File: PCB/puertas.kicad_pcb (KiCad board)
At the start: 2 copper layers, 135.8 x 85.8 mm, 70 parts, among them IC1 MAX3051ESA+, IC2 IR2175STRPBF, J1 DE9_Pins_MountingHoles, J12 motor_dc, J2 ICSP, J3 DE9_Plug_MountingHoles, J4 Conn_Coaxial, J5 BAT_CONN, J6 Conn_01x03, J7 DOOR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

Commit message: layout pre
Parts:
- moved D5 6.83 mm to (148.8, 109.5)
- moved C10 4.21 mm to (152.7, 105.2)
- moved C13 3.89 mm to (157.5, 102.9)
- moved C9 3.75 mm to (176.8, 83.1)
- moved R9 1.52 mm to (127.3, 126.0), turned to -90 degrees
- moved R2 1.04 mm to (166.1, 117.3)
- moved R17 0.86 mm to (171.2, 74.9)
- moved R12 0.65 mm to (149.1, 74.7), turned to 180 degrees
- moved R10 0.39 mm to (117.5, 62.7)
- moved R16 0.06 mm to (159.3, 74.9)
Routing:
- net /motores/DC2: track 0.00 -> 58.2 mm
- net UP: track 0.00 -> 52.7 mm
- net CLOSE: track 0.00 -> 52.1 mm
- net DOWN: track 0.00 -> 50.7 mm
- net OPEN: track 0.00 -> 47.5 mm
- net Net-(Q3-G): track 0.00 -> 41.7 mm
- net Net-(D5-K): track 0.00 -> 41.4 mm
- net GND: track 0.00 -> 37.2 mm, vias 0 -> 30
- net Net-(IC2-VIN+): track 0.00 -> 34.8 mm, vias 0 -> 1
- net Net-(Q2-G): track 0.00 -> 32.7 mm
- net Net-(Q1-G): track 0.00 -> 31.5 mm
- net Net-(D4-K): track 0.00 -> 29.2 mm, vias 0 -> 2
- net Net-(D2-K): track 6.26 -> 34.4 mm
- net /motores/LIN2: track 0.00 -> 26.3 mm
- net Net-(Q4-G): track 0.00 -> 25.4 mm
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
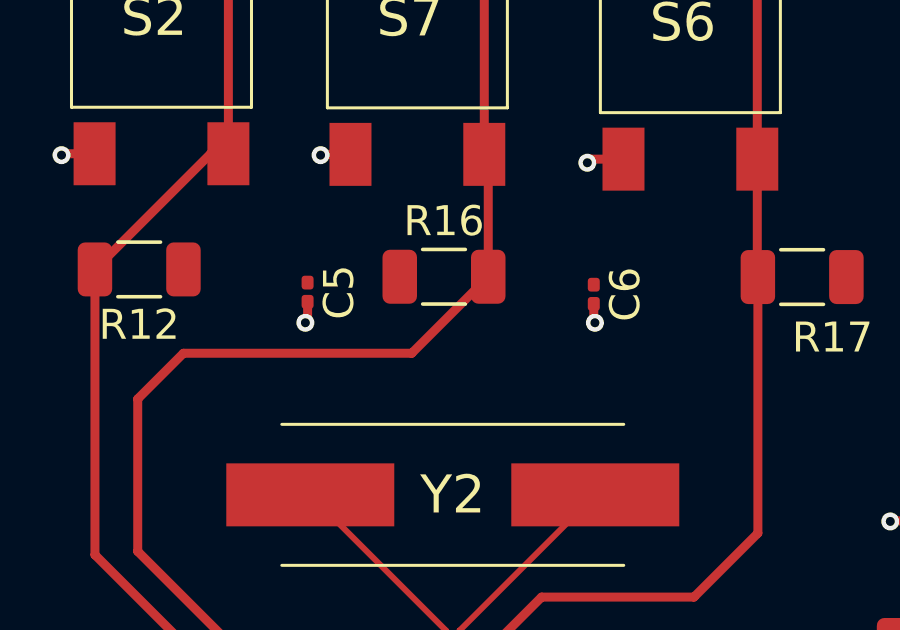
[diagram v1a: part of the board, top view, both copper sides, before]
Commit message: Fixed labels and ERC errors
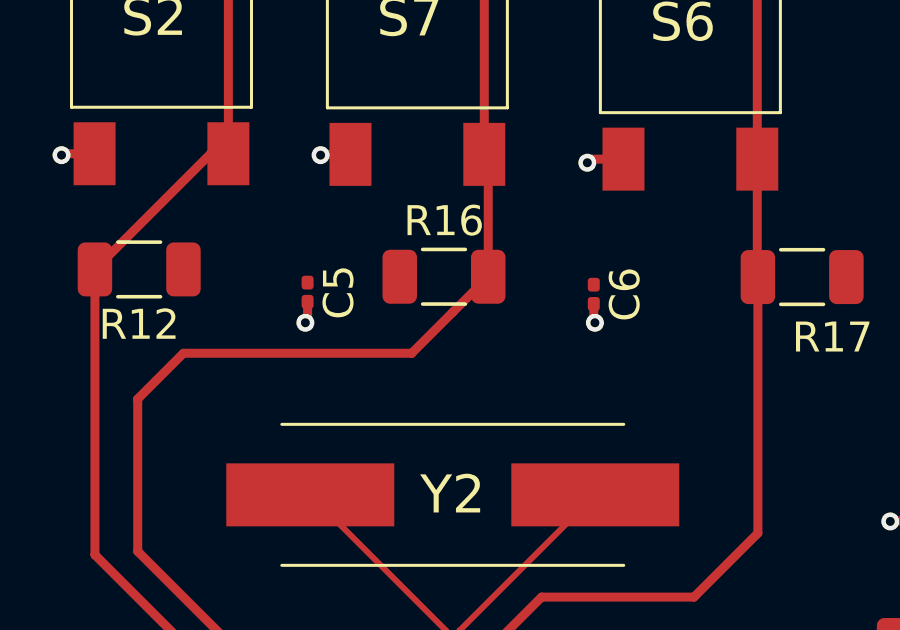
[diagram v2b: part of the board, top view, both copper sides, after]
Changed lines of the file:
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@@
 			(psa4output no)
 			(plot_black_and_white yes)
+			(plotinvisibletext no)
 			(sketchpadsonfab no)
 			(plotpadnumbers no)
@@
 	)
 	(segment
-		(start 162.56 85.598)
-		(end 159.77 88.388)
+		(start 169.77 74.93)
+		(end 169.77 83.468)
 		(width 0.3)
 		(layer "F.Cu")
@@
 	)
 	(segment
-		(start 169.77 74.93)
-		(end 169.77 83.468)
-		(width 0.3)
-		(layer "F.Cu")
-		(net 52)
-	)
-	(segment
-		(start 169.77 83.468)
-		(end 167.64 85.598)
+		(start 162.56 85.598)
+		(end 159.77 88.388)
 		(width 0.3)
 		(layer "F.Cu")
@@
 	)
 	(segment
+		(start 169.77 83.468)
+		(end 167.64 85.598)
+		(width 0.3)
+		(layer "F.Cu")
+		(net 52)
+	)
+	(segment
 		(start 169.75 74.91)
 		(end 169.77 74.93)
@@
 	(segment
 		(start 160.782 74.92)
-		(end 158.232 77.47)
+		(end 159.601 76.101)
 		(width 0.3)
 		(layer "F.Cu")
@@
 		(width 0.3)
 		(layer "F.Cu")
+		(net 54)
+	)
+	(segment
+		(start 159.601 76.101)
+		(end 158.232 77.47)
+		(width 0.3)
+		(layer "F.Cu")

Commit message: ADDED footprint RFID lector
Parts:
- added J10: Conn_01x03, Connector_PinHeader_2.54mm:PinHeader_1x03_P2.54mm_Vertical, F.Cu at (218.4, 49.5)
- added J11: Conn_01x03, Connector_PinHeader_2.54mm:PinHeader_1x03_P2.54mm_Vertical, F.Cu at (206.9, 49.0)
- added U6: ~, CREATED:DLP-RFID2, F.Cu at (207.0, 126.2)
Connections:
- net Net-(D4-K) renamed /motores/VB
- net Net-(D5-K) renamed /motores/VS
- net Net-(IC2-VIN+) renamed /motores/VIN+
- net Net-(Q1-G) renamed /motores/R_MOSL1
- net Net-(Q2-G) renamed /motores/R_MOSL2
- net Net-(Q3-G) renamed /motores/R_MOSDC1
- net Net-(Q4-G) renamed /motores/R_MOSDC2
- R12 pad 2: OPEN -> /Circuito Digital/OPEN_DOOR
- R13 pad 2: CLOSE -> /Circuito Digital/CLOSE_DOOR
- R16 pad 2: UP -> /Circuito Digital/RISE
- R17 pad 2: DOWN -> /Circuito Digital/FALL
- S2 pad 3: OPEN -> /Circuito Digital/OPEN_DOOR
- S2 pad 4: OPEN -> /Circuito Digital/OPEN_DOOR
- S3 pad 3: CLOSE -> /Circuito Digital/CLOSE_DOOR
- S3 pad 4: CLOSE -> /Circuito Digital/CLOSE_DOOR
- S6 pad 3: DOWN -> /Circuito Digital/FALL
- S6 pad 4: DOWN -> /Circuito Digital/FALL
- S7 pad 3: UP -> /Circuito Digital/RISE
- S7 pad 4: UP -> /Circuito Digital/RISE
- U1 pad 2: /Circuito Digital/L_DC -> L_DC
- U1 pad 21: /Circuito Digital/FINAL_ALTO -> FINAL_ALTO
- U1 pad 22: /Circuito Digital/SENSOR -> SENSOR
- U1 pad 25: /Circuito Digital/FINAL_BAJO -> FINAL_BAJO
- U1 pad 3: /Circuito Digital/R_DC -> R_DC
- U1 pad 4: /Circuito Digital/L_LIN -> L_LIN
- U1 pad 5: /Circuito Digital/R_LIN -> R_LIN

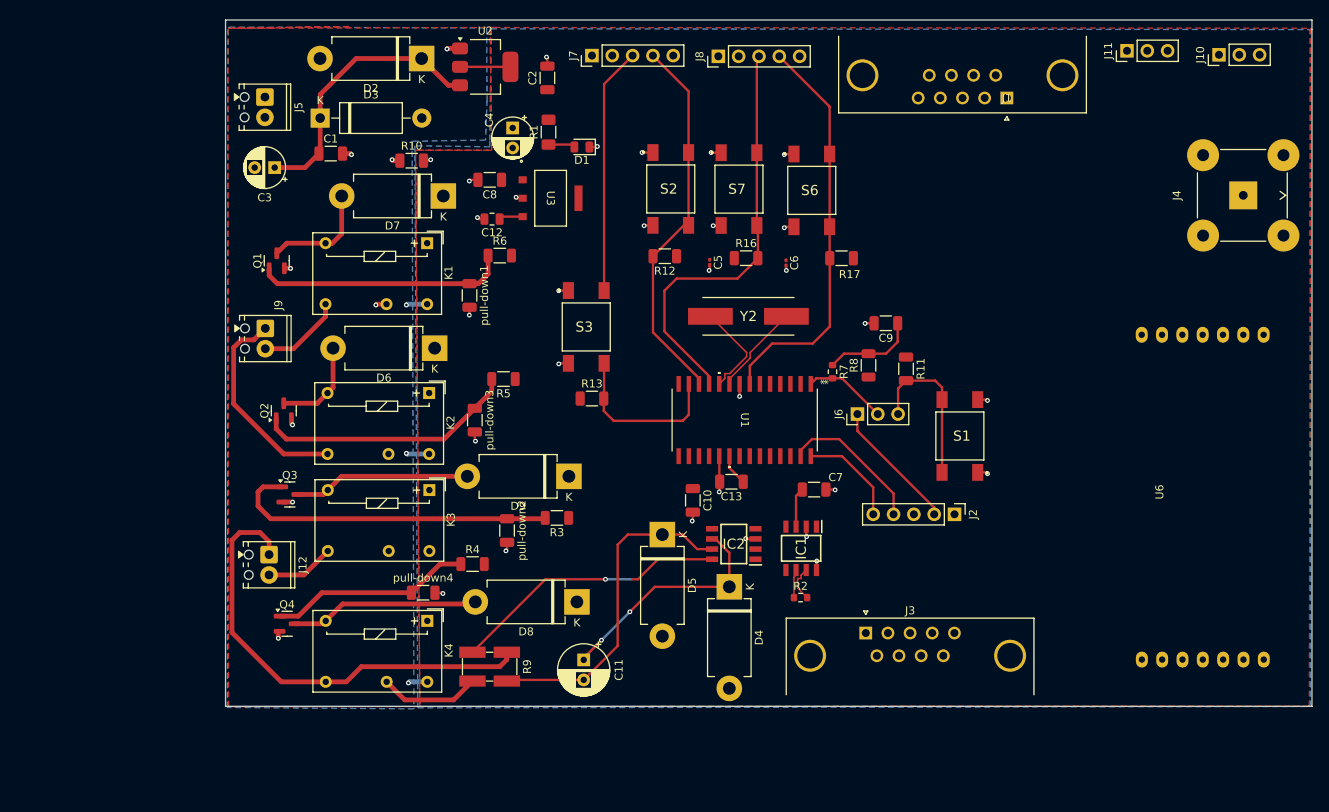
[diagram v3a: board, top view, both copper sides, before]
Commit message: layout v2, reglas jlcpcb
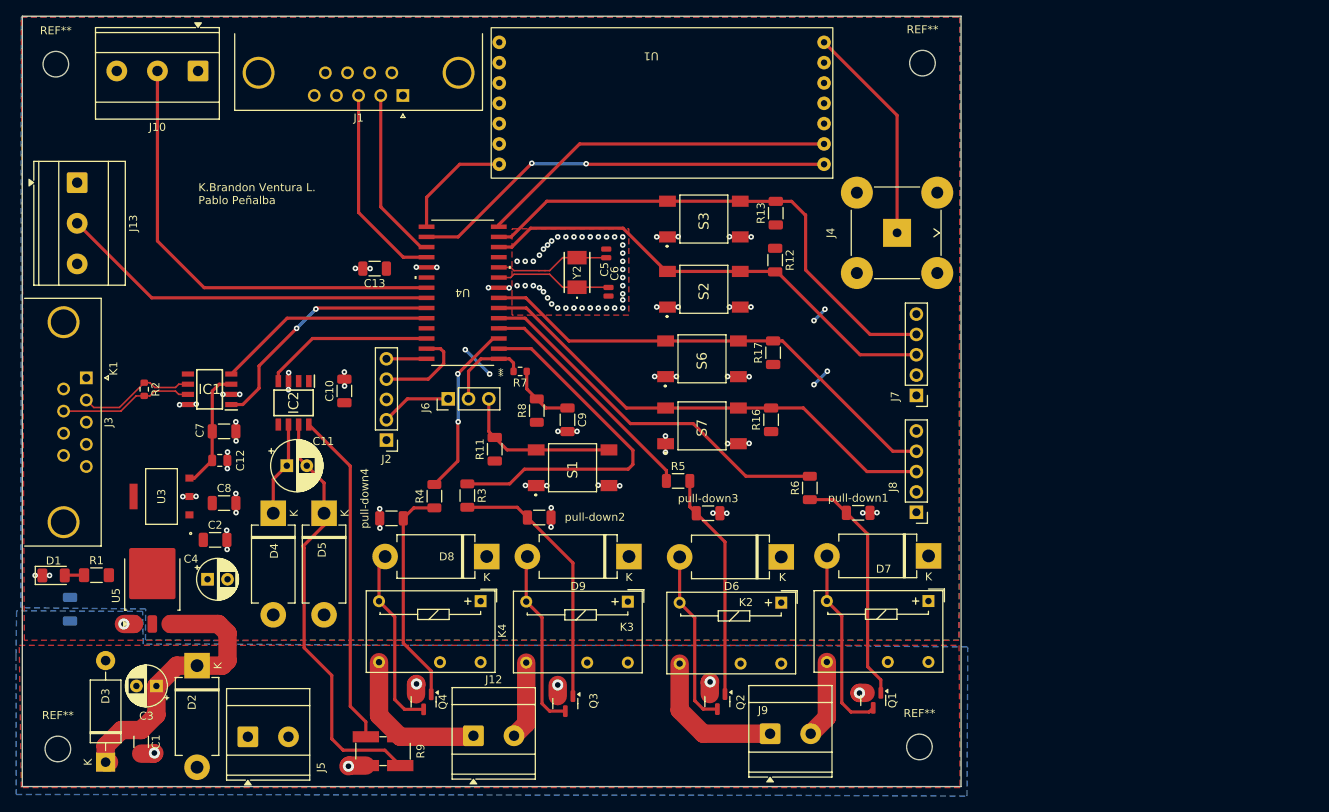
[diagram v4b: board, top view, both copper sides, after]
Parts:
- removed J11: Conn_01x03, Connector_PinHeader_2.54mm:PinHeader_1x03_P2.54mm_Vertical
- removed U2: lm1117-5V, Package_TO_SOT_SMD:SOT-223-3_TabPin2
- removed U6: ~, CREATED:DLP-RFID2
- added J13: FINAL_BAJO, TerminalBlock_Phoenix:TerminalBlock_Phoenix_MKDS-3-3-5.08_1x03_P5.08mm_Horizontal, F.Cu at (75.7, 65.5)
- added REF**: MountingHole_3.2mm_M3, MountingHole:MountingHole_3.2mm_M3, F.Cu at (73.3, 136.3)
- added REF**: MountingHole_3.2mm_M3, MountingHole:MountingHole_3.2mm_M3, F.Cu at (181.0, 136.0)
- added REF**: MountingHole_3.2mm_M3, MountingHole:MountingHole_3.2mm_M3, F.Cu at (181.4, 50.5)
- added REF**: MountingHole_3.2mm_M3, MountingHole:MountingHole_3.2mm_M3, F.Cu at (73.0, 50.7)
- added U4: PIC18F2580T-I/SO, PIC18F2580T_I_SO:SOIC28-W_MC_MCH, F.Cu at (123.9, 79.2)
- added U5: LM1117DT-5.0, Package_TO_SOT_SMD:TO-252-3_TabPin2, F.Cu at (85.1, 115.6)
- C5, C6: footprint Capacitor_SMD:C_0201_0603Metric -> Capacitor_SMD:C_0504_1310Metric
- D1: footprint LED_SMD:LED_0805_2012Metric -> LED_SMD:LED_1206_3216Metric
- J1: value DE9_Pins_MountingHoles -> DE9_USART
- J10: value Conn_01x03 -> FINAL_ALTO; footprint Connector_PinHeader_2.54mm:PinHeader_1x03_P2.54mm_Vertical -> TerminalBlock_Phoenix:TerminalBlock_Phoenix_MKDS-3-3-5.08_1x03_P5.08mm_Horizontal
- J12, J5, J9: footprint TerminalBlock_Phoenix:TerminalBlock_Phoenix_MPT-0,5-2-2.54_1x02_P2.54mm_Horizontal -> TerminalBlock_Phoenix:TerminalBlock_Phoenix_MKDS-3-2-5.08_1x02_P5.08mm_Horizontal
- J3: value DE9_Plug_MountingHoles -> DE9_CAN
- J6: value Conn_01x03 -> PROG
- R10: moved to B.Cu
- U1: value PIC18F2580T-I/SO -> ~; footprint PIC18F2580T_I_SO:SOIC28-W_MC_MCH -> DLP-RFID2:DLP-RFID2
- Y2: value ABLS -> AA-8.000MALV-T; footprint ABLS8000MHZB2T:ABLS8000MHZB2T -> AA-8.000MALV-T:AA8000MALVT
- moved J10 127.6 mm to (90.8, 51.5), turned to 180 degrees
- moved J3 102.5 mm to (76.8, 89.9), turned to -90 degrees
- moved Q1 92.6 mm to (175.2, 130.2), turned to -90 degrees
- moved R2 86.1 mm to (84.1, 91.3), turned to -90 degrees
- moved D1 85.0 mm to (72.7, 114.6), turned to 0 degrees
- moved D3 84.9 mm to (79.2, 137.9), turned to 90 degrees
- moved J9 80.9 mm to (162.3, 134.4), turned to 0 degrees
- moved D2 80.9 mm to (90.7, 125.9), turned to -90 degrees
- moved J5 80.0 mm to (97.0, 134.7), turned to 0 degrees
- moved R1 79.1 mm to (78.1, 114.5), turned to 0 degrees
- moved C1 77.3 mm to (83.7, 135.4), turned to -90 degrees
- moved K1 77.0 mm to (182.1, 117.8)
- moved IC1 76.6 mm to (92.2, 91.3), turned to 180 degrees
- moved D7 75.5 mm to (182.1, 112.1)
- moved J1 75.5 mm to (116.4, 54.6)
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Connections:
- net Net-(C9-Pad1) renamed /Circuito Digital/R8_C9
- net Net-(D1-A) renamed /Regulador/R1_LED
- net Net-(D2-K) renamed /Regulador/D2_VI
- J10 pad 2: FINAL_BAJO -> FINAL_ALTO
- J7 pad 3: CLOSE -> OPEN
- J7 pad 4: OPEN -> CLOSE
- R12 pad 2: /Circuito Digital/OPEN_DOOR -> OPEN
- R13 pad 2: /Circuito Digital/CLOSE_DOOR -> CLOSE
- R16 pad 2: /Circuito Digital/RISE -> UP
- R17 pad 2: /Circuito Digital/FALL -> DOWN
- S2 pad 3: /Circuito Digital/OPEN_DOOR -> OPEN
- S2 pad 4: /Circuito Digital/OPEN_DOOR -> OPEN
- S3 pad 3: /Circuito Digital/CLOSE_DOOR -> CLOSE
- S3 pad 4: /Circuito Digital/CLOSE_DOOR -> CLOSE
- S6 pad 3: /Circuito Digital/FALL -> DOWN
- S6 pad 4: /Circuito Digital/FALL -> DOWN
- S7 pad 3: /Circuito Digital/RISE -> UP
- S7 pad 4: /Circuito Digital/RISE -> UP
- U1 pad 1: /Circuito Digital/MCLR -> /Circuito Digital/IN_RFID
- U1 pad 10: /Circuito Digital/OS- -> unconnected-(U1-P2.5-Pad10)
- U1 pad 11: UP -> unconnected-(U1-P2.7-Pad11)
- U1 pad 12: OPEN -> GND
- U1 pad 13: CLOSE -> /Circuito Digital/RF
- U1 pad 14: /Circuito Digital/RESET_RFID -> GND
- U1 pad 2: L_DC -> /Circuito Digital/OUT_RFID
- U1 pad 3: R_DC -> /Circuito Digital/RESET_RFID
- U1 pad 4: L_LIN -> GND
- U1 pad 5: R_LIN -> unconnected-(U1-P1.2-Pad5)
- U1 pad 7: DOWN -> +5V
- U1 pad 8: GND -> unconnected-(U1-P2.4-Pad8)
- U1 pad 9: /Circuito Digital/OS+ -> GND
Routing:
- net FINAL_ALTO: track 0.00 -> 57.3 mm
- net /Circuito Digital/IN_RFID: track 0.00 -> 54.3 mm, vias 0 -> 2
- net FINAL_BAJO: track 0.00 -> 47.5 mm
- net L_LIN: track 0.00 -> 47.1 mm
- net L_DC: track 0.00 -> 45.5 mm
- net /Circuito Digital/RESET_RFID: track 0.00 -> 45.1 mm
- net /motores/DC2: track 58.2 -> 19.6 mm
- net /Circuito Digital/CAN_TX: track 0.00 -> 31.0 mm, vias 0 -> 2
- net R_LIN: track 0.00 -> 29.6 mm
- net GND: track 37.2 -> 65.1 mm, vias 30 -> 96
- net /Circuito Digital/RF: track 0.00 -> 27.6 mm
- net /Circuito Digital/CAN_RX: track 0.00 -> 27.3 mm
- net /Circuito Digital/USART_RX: track 0.00 -> 25.4 mm
- net R_DC: track 0.00 -> 22.0 mm, vias 0 -> 2
- net /Circuito Digital/USART_TX: track 0.00 -> 21.7 mm
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- added copper zone on F.Cu, net GND
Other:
- board size 135.8 x 85.8 mm -> 117.3 x 96.3 mm
- board text added: "K.Brandon Ventura L. Pablo Peñalba"

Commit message: ancho de pista de gnd, corrección de ruteado
corrección de separación de plano de +5V, ancho de pista coincidente con gnd
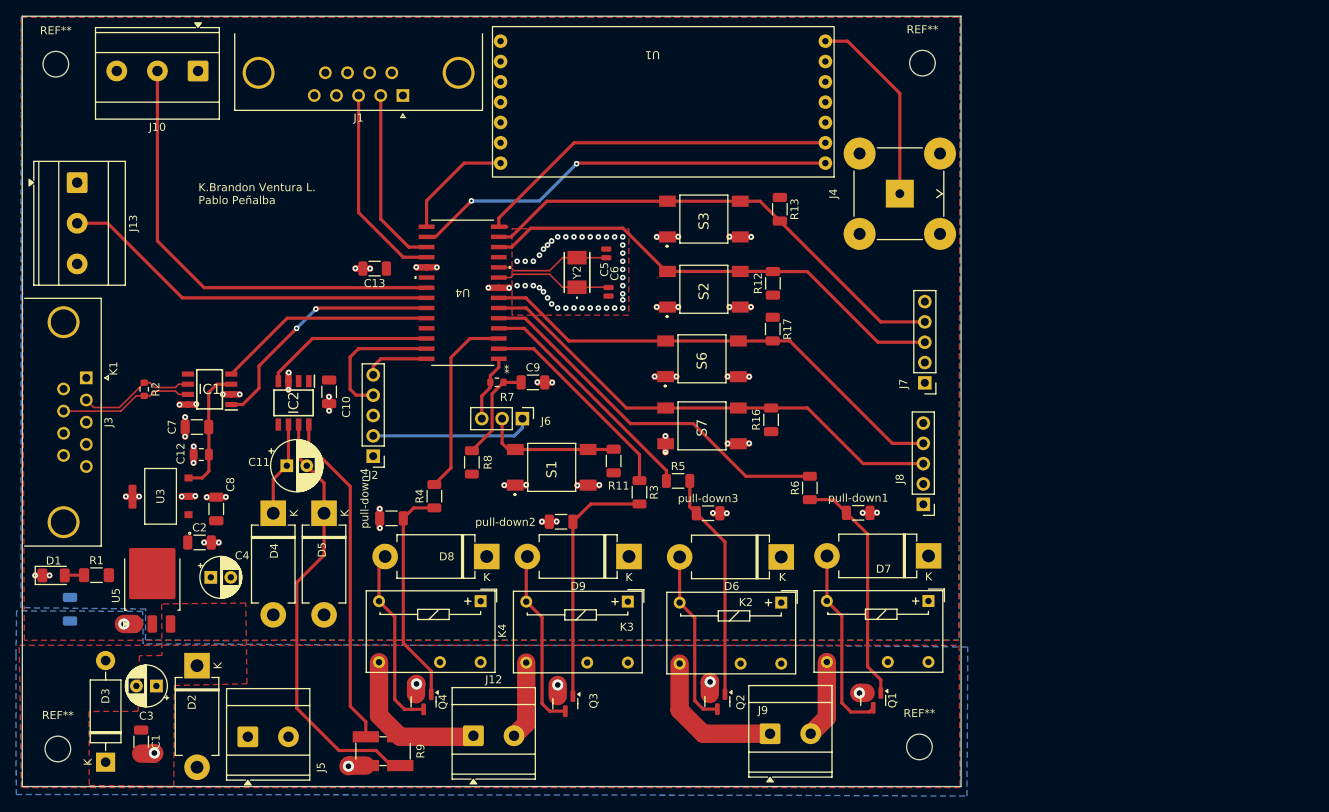
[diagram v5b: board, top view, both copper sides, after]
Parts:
- U1: value ~ -> DLP-RFID2
- U3: footprint LT1121IST:SOT-223_ST_LIT -> LT1121IST-3.3-TRPBF:SOT-223_ST_LIT
- moved R3 21.5 mm to (146.0, 104.2)
- moved R11 14.9 mm to (142.8, 100.3)
- moved R8 10.4 mm to (125.0, 100.5)
- moved J6 9.60 mm to (131.3, 95.0), turned to -90 degrees
- moved C9 6.36 mm to (132.7, 90.5), turned to 0 degrees
- moved J4 4.90 mm to (178.5, 66.9)
- moved C7 3.43 mm to (90.7, 96.0), turned to 180 degrees
- moved R7 3.20 mm to (128.2, 90.4)
- moved R17 2.96 mm to (162.6, 83.8), turned to -90 degrees
- moved R12 2.92 mm to (162.7, 78.1), turned to 90 degrees
- moved pull-down2 2.78 mm to (136.2, 107.9), turned to 180 degrees
- moved S1 2.61 mm to (135.0, 101.1)
- moved J2 2.60 mm to (112.7, 99.7)
- moved C12 2.42 mm to (91.2, 99.5), turned to 180 degrees
- moved C2 1.97 mm to (91.0, 110.5)
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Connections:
- J6 pad 2: /Circuito Digital/MCLR -> /Circuito Digital/MAN_MCLR
- J6 pad 3: /Circuito Digital/MAN_MCLR -> /Circuito Digital/MCLR
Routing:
- net /Regulador/D2_VI: track 35.3 -> 0.00 mm
- net L_DC: track 45.5 -> 26.3 mm
- net /Circuito Digital/PROG_MCLR: track 8.81 -> 20.2 mm
- net +5V: track 8.82 -> 0.00 mm, vias 6 -> 0
- net /Circuito Digital/PGC: track 11.8 -> 17.2 mm
- net /Circuito Digital/R8_C9: track 8.27 -> 12.4 mm
- net CLOSE: track 65.0 -> 61.4 mm
- net /Circuito Digital/PGD: track 5.02 -> 8.13 mm
- net /Circuito Digital/RF: track 27.6 -> 24.5 mm
- net /Circuito Digital/MAN_MCLR: track 20.1 -> 17.4 mm
- net /Circuito Digital/MCLR: track 11.0 -> 8.41 mm
- net /Circuito Digital/RESET_RFID: track 45.1 -> 46.8 mm
- net /motores/R_MOSDC1: track 32.7 -> 31.0 mm
- net R_DC: track 22.0 -> 23.7 mm, vias 2 -> 0
- net /motores/VS: track 53.1 -> 54.1 mm
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- added copper zone on F.Cu, net /Regulador/D2_VI

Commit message: Update PCB
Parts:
- moved REF** 0.76 mm to (181.4, 136.7)
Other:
- board text added: "K.Brandon Ventura L. Pablo Peñalba 2024/2025"
- board text removed: "K.Brandon Ventura L. Pablo Peñalba"
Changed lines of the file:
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@@
 	)
 	(paper "A4")
+	(title_block
+		(title "PCB_puertas")
+		(date "2025-04-19")
+		(rev "4/4")
+	)
 	(layers
 		(0 "F.Cu" signal)
@@
 			(outputformat 1)
 			(mirror no)
-			(drillshape 1)
+			(drillshape 0)
 			(scaleselection 1)
-			(outputdirectory "")
+			(outputdirectory "../Gerbers/")
 		)
 	)
@@
 	(footprint "MountingHole:MountingHole_3.2mm_M3"
 		(layer "F.Cu")
-		(at 180.975 136.017)
+		(at 181.39 136.65)
 		(descr "Mounting Hole 3.2mm, no annular, M3")
 		(tags "mounting hole 3.2mm no annular m3")
@@
 		)
 		(embedded_fonts no)
+		(model "/home/ventura/Documents/Kicad/projecte/componentes/PIC18F2580T_I_SO/3d model/PIC18F2580T-I_SO.STEP"
+			(offset
+				(xyz 0 0 0)
+			)
+			(scale
+				(xyz 1 1 1)
+			)
+			(rotate
+				(xyz -90 -0 -0)
+			)
+		)
 	)
 	(footprint "Diode_THT:D_DO-201AD_P12.70mm_Horizontal"
@@
 		(layer "Edge.Cuts")
 	)
-	(gr_text "K.Brandon Ventura L.\nPablo Peñalba"
-		(at 90.84 68.28 0)
+	(gr_text "K.Brandon Ventura L.\nPablo Peñalba\n2024/2025"
+		(at 87.31 70.4 0)
 		(layer "F.SilkS")
 		(effects
 			(font
-				(size 1 1)
+				(size 1.4 1.4)
 				(thickness 0.1)
 			)
